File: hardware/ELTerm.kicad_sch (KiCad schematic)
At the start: 31 parts, among them J1 Barrel_Jack_Switch, J2 Conn_02x10_Odd_Even, J3 Conn_01x02, J4 Mini-DIN-6, J5 Conn_02x03_Odd_Even, J6 Conn_01x02, J7 DB9_Male_MountingHoles, SW1 SW_Push, U1 SY8120, U2 Pico, U3 MAX3232, U4 NC7WZ16P6X

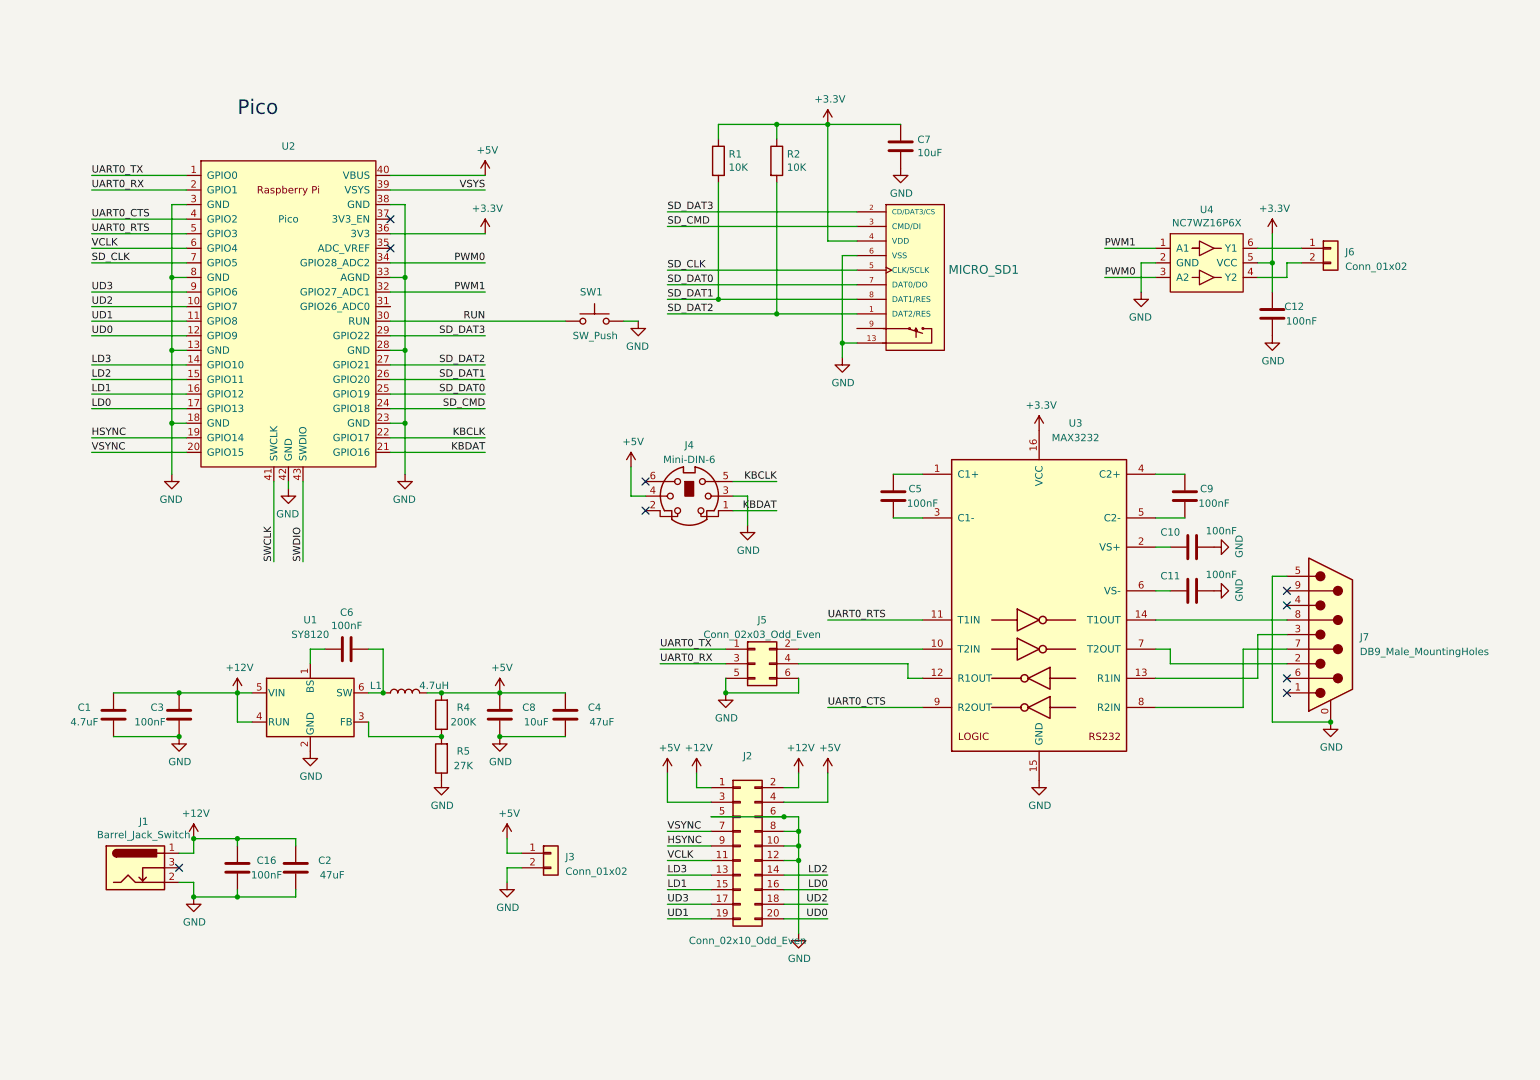
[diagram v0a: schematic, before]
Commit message: Adapt EL screen to sharp LJ64
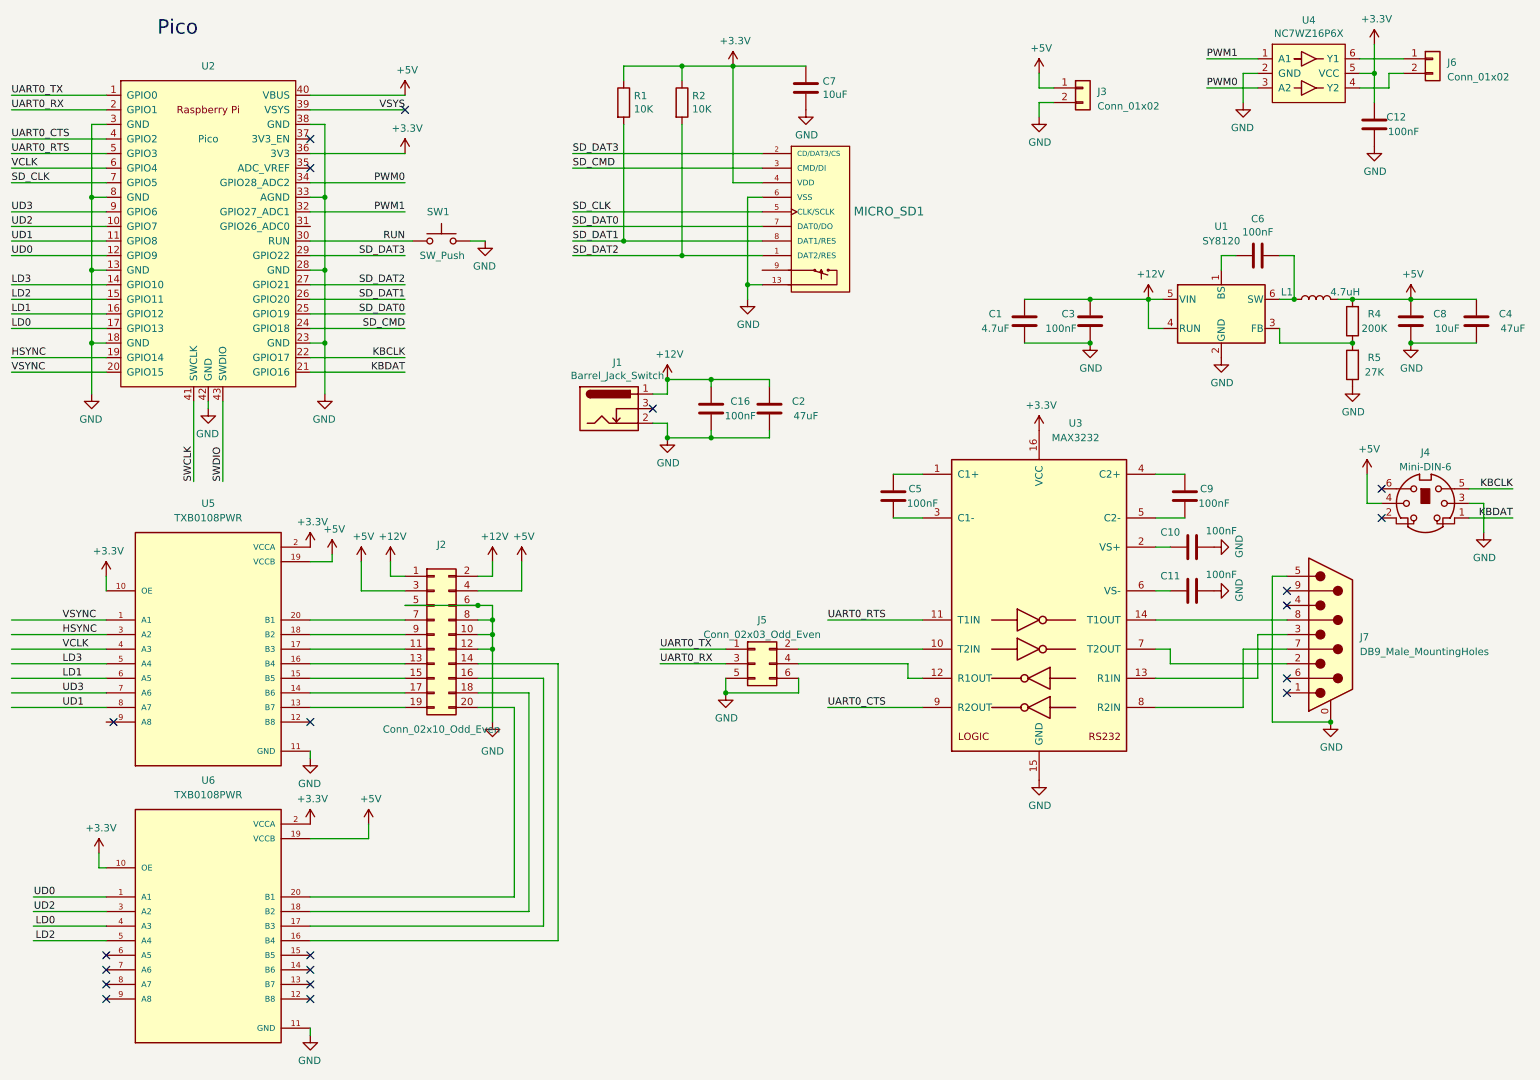
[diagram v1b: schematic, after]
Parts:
- added U5, U6: TXB0108PWR, TXB0108PWR:SOP65P640X120-20N, symbol TXB0108PWR:TXB0108PWR
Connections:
- net +3V3: now also U5.10 (OE), U5.2 (VCCA), U6.10 (OE), U6.2 (VCCA)
- net +5V: now also U5.19 (VCCB), U6.19 (VCCB)
- net GND: now also U5.11 (GND), U6.11 (GND)
- net HSYNC: now also U5.3 (A2); no longer J2.9 (Pin_9)
- net LD0: now also U6.4 (A3); no longer J2.16 (Pin_16)
- net LD1: now also U5.6 (A5); no longer J2.15 (Pin_15)
- net LD2: now also U6.5 (A4); no longer J2.14 (Pin_14)
- net LD3: now also U5.5 (A4); no longer J2.13 (Pin_13)
- net UD0: now also U6.1 (A1); no longer J2.20 (Pin_20)
- net UD1: now also U5.8 (A7); no longer J2.19 (Pin_19)
- net UD2: now also U6.3 (A2); no longer J2.18 (Pin_18)
- net UD3: now also U5.7 (A6); no longer J2.17 (Pin_17)
- net VCLK: now also U5.4 (A3); no longer J2.11 (Pin_11)
- net VSYNC: now also U5.1 (A1); no longer J2.7 (Pin_7)
- new net: J2.11 (Pin_11), U5.17 (B3)
- new net: J2.13 (Pin_13), U5.16 (B4)
- new net: J2.14 (Pin_14), U6.16 (B4)
- new net: J2.15 (Pin_15), U5.15 (B5)
- new net: J2.16 (Pin_16), U6.17 (B3)
- new net: J2.17 (Pin_17), U5.14 (B6)
- new net: J2.18 (Pin_18), U6.18 (B2)
- new net: J2.19 (Pin_19), U5.13 (B7)
- new net: J2.20 (Pin_20), U6.20 (B1)
- new net: J2.7 (Pin_7), U5.20 (B1)
- new net: J2.9 (Pin_9), U5.18 (B2)
- no-connect marks 9 -> 20
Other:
- moved on the sheet: C1, C12, C16, C2, C3, C4, C6, C7, C8, J1, J2, J3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
